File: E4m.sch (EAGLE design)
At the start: 78 parts, among them Q1 IRL540, Q2 IRL540, Q3 tip120

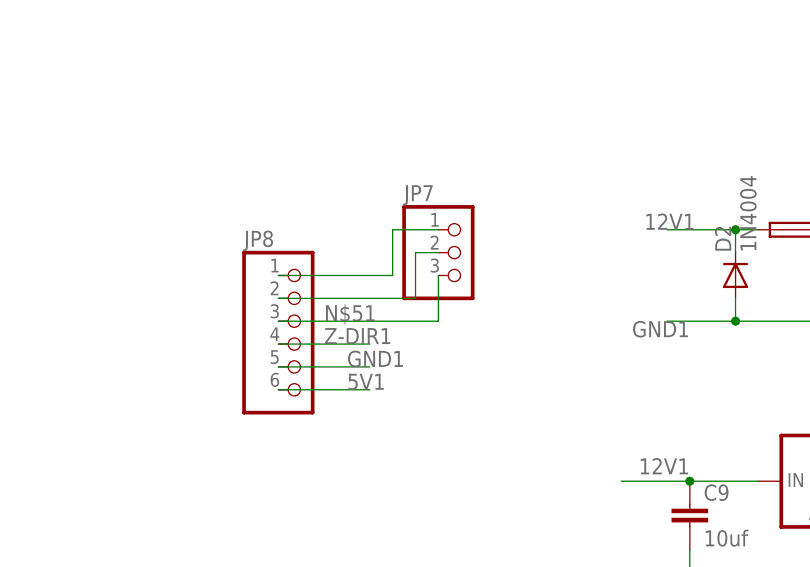
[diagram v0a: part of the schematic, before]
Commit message: Add files via upload
reposition several elements for better routing
routing done

todo 1: fix 2 holes used for mounting/fixing the board
todo 2: check all drc on file
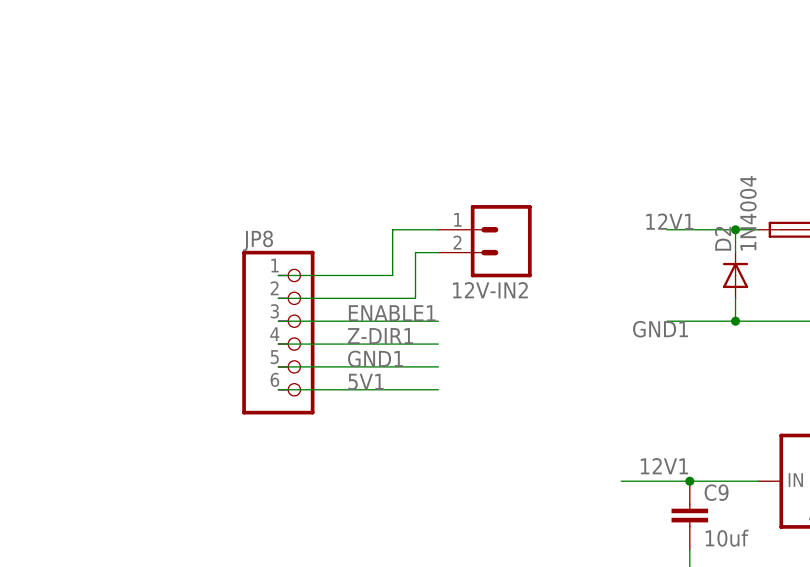
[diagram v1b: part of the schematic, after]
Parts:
- removed JP7: (no value), pinhead:PINHD-1X3
- added 12V-IN2: (no value), SparkFun:M02PTH
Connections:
- removed net N$51: JP7.3, JP8.3
- net ENABLE1: now also JP8.3
- net N$52: now also 12V-IN2.2; no longer JP7.2
- net N$53: now also 12V-IN2.1; no longer JP7.1
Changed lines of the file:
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@@
 <part name="C9" library="eagle-ltspice" deviceset="C" device="C0603" value="10uf"/>
 <part name="C10" library="eagle-ltspice" deviceset="C" device="C0603" value="100uf"/>
-<part name="JP7" library="pinhead" deviceset="PINHD-1X3" device=""/>
 <part name="JP8" library="pinhead" deviceset="PINHD-1X6" device=""/>
 <part name="Q1" library="smootietransistor-power" deviceset="IRF540" device="" value="IRL540"/>
@@
 <part name="LED2" library="RepRapjr" deviceset="LED" device="CHIP-LED0805"/>
 <part name="Q3" library="smootietransistor-power" deviceset="IRF540" device="" value="tip120"/>
+<part name="12V-IN2" library="SparkFun" deviceset="M02" device="PTH"/>
 </parts>
 <sheets>
@@
 <instance part="C9" gate="G$1" x="167.64" y="190.5"/>
 <instance part="C10" gate="G$1" x="195.58" y="190.5"/>
-<instance part="JP7" gate="A" x="142.24" y="218.44"/>
 <instance part="JP8" gate="A" x="124.46" y="208.28"/>
 <instance part="Q1" gate="G$1" x="88.9" y="-27.94"/>
@@
 <instance part="LED2" gate="G$1" x="99.06" y="48.26"/>
 <instance part="Q3" gate="G$1" x="121.92" y="5.08"/>
+<instance part="12V-IN2" gate="G$1" x="147.32" y="220.98" rot="R180"/>
 </instances>
 <busses>
@@
 </segment>
 <segment>
-<wire x1="121.92" y1="205.74" x2="132.08" y2="205.74" width="0.1524" layer="91"/>
+<wire x1="121.92" y1="205.74" x2="139.7" y2="205.74" width="0.1524" layer="91"/>
 <label x="129.54" y="205.74" size="1.778" layer="95"/>
 <pinref part="JP8" gate="A" pin="5"/>
@@
 <net name="5V1" class="0">
 <segment>
-<wire x1="121.92" y1="203.2" x2="132.08" y2="203.2" width="0.1524" layer="91"/>
+<wire x1="121.92" y1="203.2" x2="139.7" y2="203.2" width="0.1524" layer="91"/>
 <label x="129.54" y="203.2" size="1.778" layer="95"/>
 <pinref part="JP8" gate="A" pin="6"/>
@@
 <pinref part="U$6" gate="G$1" pin="EN"/>
 </segment>
+<segment>
+<wire x1="121.92" y1="210.82" x2="139.7" y2="210.82" width="0.1524" layer="91"/>
+<label x="129.54" y="210.82" size="1.778" layer="95"/>
+<pinref part="JP8" gate="A" pin="3"/>
+</segment>
 </net>
 <net name="Z-DIR1" class="0">
 <segment>
-<wire x1="121.92" y1="208.28" x2="132.08" y2="208.28" width="0.1524" layer="91"/>
-<label x="127" y="208.28" size="1.778" layer="95"/>
+<wire x1="121.92" y1="208.28" x2="139.7" y2="208.28" width="0.1524" layer="91"/>
+<label x="129.54" y="208.28" size="1.778" layer="95"/>
 <pinref part="JP8" gate="A" pin="4"/>
 </segment>
@@
 <wire x1="22.86" y1="198.12" x2="15.24" y2="198.12" width="0.1524" layer="91"/>
 <label x="15.24" y="198.12" size="1.778" layer="95"/>
-</segment>
-</net>
-<net name="N$51" class="0">
-<segment>
-<wire x1="121.92" y1="210.82" x2="139.7" y2="210.82" width="0.1524" layer="91"/>
-<label x="127" y="210.82" size="1.778" layer="95"/>
-<pinref part="JP7" gate="A" pin="3"/>
-<wire x1="139.7" y1="210.82" x2="139.7" y2="215.9" width="0.1524" layer="91"/>
-<pinref part="JP8" gate="A" pin="3"/>
 </segment>
 </net>
@@
 <segment>
 <wire x1="121.92" y1="215.9" x2="134.62" y2="215.9" width="0.1524" layer="91"/>
-<pinref part="JP7" gate="A" pin="1"/>
 <wire x1="134.62" y1="215.9" x2="134.62" y2="220.98" width="0.1524" layer="91"/>
 <wire x1="134.62" y1="220.98" x2="139.7" y2="220.98" width="0.1524" layer="91"/>
 <pinref part="JP8" gate="A" pin="1"/>
+<pinref part="12V-IN2" gate="G$1" pin="1"/>
 </segment>
 </net>
 <net name="N$52" class="0">
 <segment>
-<pinref part="JP7" gate="A" pin="2"/>
 <wire x1="139.7" y1="218.44" x2="137.16" y2="218.44" width="0.1524" layer="91"/>
 <wire x1="137.16" y1="218.44" x2="137.16" y2="213.36" width="0.1524" layer="91"/>
 <wire x1="137.16" y1="213.36" x2="121.92" y2="213.36" width="0.1524" layer="91"/>
 <pinref part="JP8" gate="A" pin="2"/>
-</segment>
-</net>
+<pinref part="12V-IN2" gate="G$1" pin="2"/>
+</segment>
+</net>

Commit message: last verified
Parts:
- removed E-MOT1, X-MOT1, X-MOT2, Y-MOT1, Z-MOT3: (no value), RepRapjr:PINHD-1X4
- removed JP1, JP2, JP3: (no value), pinhead:PINHD-1X3
- removed U$4: PCF8575TS, Ferduino:PCF8575TS
- added ANALOG: (no value), RepRapjr:PINHD-1X4
- added IC1: MCP23017SS, adafruit:MCP23017SS
- added LED3: (no value), RepRapjr:LEDCHIP-LED0805
- added R5: 22R, adafruit:R-US_R0805
- added R6: 10k, adafruit:R-US_R0805
- added X-S, Y-S, Z-S: (no value), pinhead:PINHD-1X3
- E-MOT, X-MOT, Y-MOT, Z-MOT: device RepRapjr:PINHD-1X4 -> adafruit:PINHD-1X8CLEANBIG
- Q3: value tip120 -> IRL540
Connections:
- removed net N$61: U$3.2A, Y-MOT.2, Y-MOT1.2
- removed net N$62: U$3.1A, Y-MOT.3, Y-MOT1.3
- removed net N$63: U$3.1B, Y-MOT.4, Y-MOT1.4
- removed net N$68: U$9.2B, Z-MOT.1, Z-MOT3.1
- removed net N$69: U$9.2A, Z-MOT.2, Z-MOT3.2
- removed net N$70: U$9.1A, Z-MOT.3, Z-MOT3.3
- removed net N$71: U$9.1B, Z-MOT.4, Z-MOT3.4
- new net N$1: LED3.A, R5.1
- new net N$12: U$1.1B, X-MOT.4, X-MOT.8
- new net N$14: U$1.1A, X-MOT.3, X-MOT.7
- new net N$15: U$1.2A, X-MOT.2, X-MOT.6
- new net N$16: U$1.2B, X-MOT.1, X-MOT.5
- new net N$17: U$9.1B, Z-MOT.4, Z-MOT.8
- new net N$3: AUX2.2, IC1.GPB6
- new net N$51: E-MOT.3, E-MOT.7, U$2.1A
- net 12V: now also FAN.1, R5.2; no longer FAN.2
- net 3V3: now also IC1.VDD; no longer U$4.VCC
- net 5V: now also X-S.3, Y-S.3, Z-S.3; no longer JP1.3, JP2.3, JP3.3
- net ANALOG: now also ANALOG.2, ANALOG.4; no longer X-MOT2.2, X-MOT2.4
- net AUX2: now also IC1.GPB7; no longer U$4.P17
- net E-DIR: now also IC1.GPA3; no longer U$4.P03
- net ENABLE: now also IC1.GPA4; no longer U$4.P04
- net GND: now also IC1.A0, IC1.A1, IC1.A2, IC1.VSS, R6.2, X-S.2, Y-S.2, Z-S.2; no longer JP1.2, JP2.2, JP3.2, U$4.A0, U$4.A1, U$4.A2, U$4.GND
- net N$10: now also U$3.2A, Y-MOT.2, Y-MOT.6; no longer E-MOT.3, E-MOT1.3, U$2.1A
- net N$11: now also U$3.2B, Y-MOT.1, Y-MOT.5; no longer E-MOT.4, E-MOT1.4, U$2.1B
- net N$18: now also FAN.2, LED3.C; no longer FAN.1
- net N$19: now also IC1.GPB2; no longer U$4.P12
- net N$20: now also U$9.1A, Z-MOT.3, Z-MOT.7; no longer AUX2.2, U$4.P16
- net N$21: now also IC1.GPB5; no longer U$4.P15
- net N$22: now also IC1.GPB4; no longer U$4.P14
- net N$26: now also IC1.GPB3; no longer U$4.P13
- net N$27: now also R6.1
- net N$46: now also U$9.2A, Z-MOT.2, Z-MOT.6; no longer U$1.2B, X-MOT.1, X-MOT1.1
- net N$48: now also U$9.2B, Z-MOT.1, Z-MOT.5; no longer U$1.2A, X-MOT.2, X-MOT1.2
- net N$50: now also E-MOT.4, E-MOT.8, U$2.1B; no longer U$1.1A, X-MOT.3, X-MOT1.3
- net N$55: now also E-MOT.2, E-MOT.6, U$2.2A; no longer U$1.1B, X-MOT.4, X-MOT1.4
- net N$60: now also E-MOT.1, E-MOT.5, U$2.2B; no longer U$3.2B, Y-MOT.1, Y-MOT1.1
- net N$8: now also U$3.1B, Y-MOT.4, Y-MOT.8; no longer E-MOT.1, E-MOT1.1, U$2.2B
- net N$9: now also U$3.1A, Y-MOT.3, Y-MOT.7; no longer E-MOT.2, E-MOT1.2, U$2.2A
- net S-A0: now also ANALOG.3, IC1.GPB0; no longer U$4.P10, X-MOT2.3
- net S-A1: now also ANALOG.1, IC1.GPB1; no longer U$4.P11, X-MOT2.1
- net SCL: now also IC1.SCL; no longer U$4.SCL
- net SDA: now also IC1.SDA; no longer U$4.SDA
- net X-DIR: now also IC1.GPA0; no longer U$4.P00
- net X-STOP: now also IC1.GPA5, X-S.1; no longer JP1.1, U$4.P05
- net Y-DIR: now also IC1.GPA1; no longer U$4.P01
- net Y-STOP: now also IC1.GPA6, Y-S.1; no longer JP2.1, U$4.P06
- net Z-DIR: now also IC1.GPA2; no longer U$4.P02
- net Z-STOP: now also IC1.GPA7, Z-S.1; no longer JP3.1, U$4.P07
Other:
- moved on the sheet: 12V-IN, AUX1, AUX2, C5, C6, D1, FAN, HB, HE, JP4, LED1, LED2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

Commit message: ops
added servo output and panelized 100x100
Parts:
- added JP1, JP2: (no value), adafruit:PINHD-1X3CB
- AUX1, AUX2, JP4, X-S, Y-S, Z-S: device pinhead:PINHD-1X3 -> adafruit:PINHD-1X3CB
- JP8: device pinhead:PINHD-1X6 -> adafruit:PINHD-1X6
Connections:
- net 5V: now also JP2.1, JP2.2, JP2.3
- net GND: now also JP1.1, JP1.2, JP1.3

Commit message: another update
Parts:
- removed 12V-IN2, EXTRA: (no value), SparkFun:M02PTH
- removed AUX1, AUX2: (no value), adafruit:PINHD-1X3CB
- removed R1, R11, R13, R2, R3: 100k, adafruit:R-US_R0805
- removed R8: 11, RepRapjr:PTCFUSE
- added JP3: (no value), adafruit:PINHD-1X1CB
- added PAD1, PAD2, PAD3, PAD4, PAD5, PAD6: WIREPADSMD1,27-254, wirepad:WIREPADSMD1,27-254
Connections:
- removed net N$47: 12V-IN1.1, R8.1
- removed net N$52: 12V-IN2.2, JP8.2
- removed net N$53: 12V-IN2.1, JP8.1
- new net 3V31: JP3.1, SJ15.1, SJ17.1, SJ18.1, U$6.VDD
- net 12V1: now also 12V-IN1.1; no longer R8.2
- net 3V3: now also SJ10.1, SJ11.1, SJ12.1, SJ13.1, SJ2.1, SJ3.1, SJ4.1, SJ5.1, SJ6.1, SJ7.1, SJ8.1, SJ9.1, U$1.VDD, U$2.VDD, U$3.VDD, U$9.VDD
- net 5V: no longer SJ10.1, SJ11.1, SJ12.1, SJ13.1, SJ2.1, SJ3.1, SJ4.1, SJ5.1, SJ6.1, SJ7.1, SJ8.1, SJ9.1, U$1.VDD, U$2.VDD, U$3.VDD, U$9.VDD
- net 5V1: no longer SJ15.1, SJ17.1, SJ18.1, U$6.VDD
- net ANALOG: now also ANALOG.1; no longer ANALOG.2
- net AUX2: now also PAD1.P; no longer AUX2.1
- net E-DIR: no longer EXTRA.2
- net E-STEP: now also U$5.D0; no longer EXTRA.1, U$5.D1
- net GND: no longer R1.2, R11.2, R13.2, R3.2
- net GND1: no longer R2.2
- net HB0: now also JP4.1; no longer JP4.2
- net HE0: now also JP4.2; no longer JP4.1
- net N$19: now also PAD6.P; no longer AUX1.3
- net N$21: now also PAD2.P; no longer AUX2.3
- net N$22: now also PAD4.P; no longer AUX1.1
- net N$26: now also PAD5.P; no longer AUX1.2
- net N$3: now also PAD3.P; no longer AUX2.2
- net N$35: no longer R3.1
- net N$40: no longer R2.1
- net N$59: no longer R11.1
- net N$67: no longer R13.1
- net N$7: no longer R1.1
- net S-A1: now also ANALOG.2; no longer ANALOG.1
- net SCL: now also U$5.D1; no longer U$5.D0
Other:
- moved on the sheet: JP2
